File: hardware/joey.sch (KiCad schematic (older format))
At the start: 0 parts

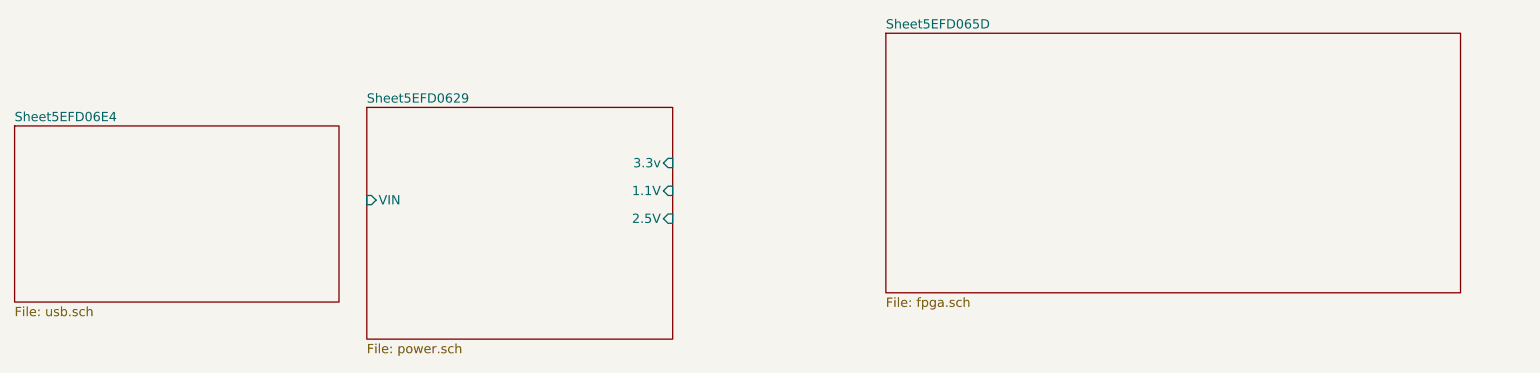
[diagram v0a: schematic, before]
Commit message: Finish FTDI schematic, add datasheets
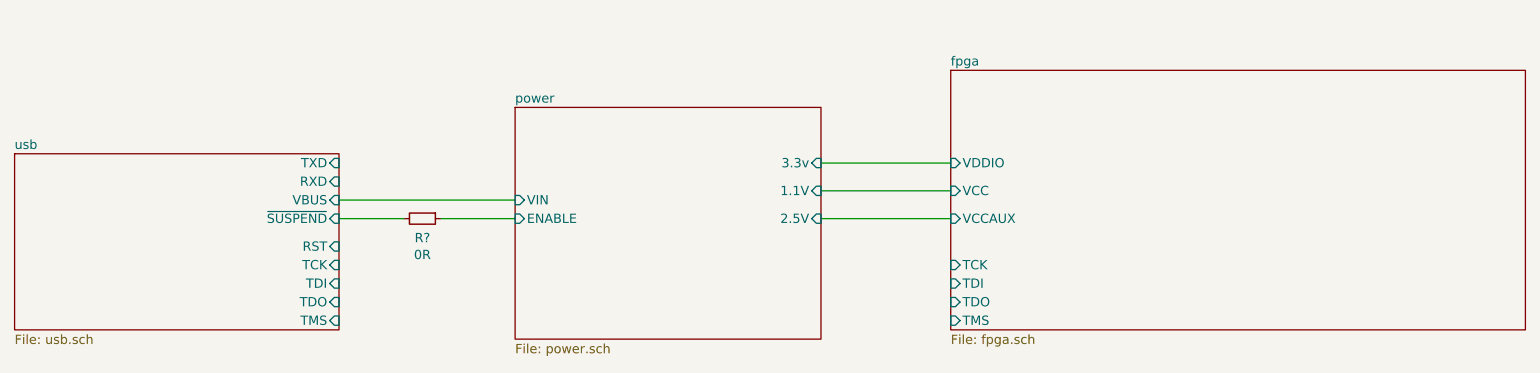
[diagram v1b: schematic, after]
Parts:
- added R?: 0R, symbol Device:R_Small
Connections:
- new net power/ENABLE: R?.1
- new net usb/~SUSPEND~: R?.2
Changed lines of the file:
@@
 $EndDescr
 $Sheet
-S 2650 2450 1650 1250
+S 3450 2450 1650 1250
 U 5EFD062A
-F0 "Sheet5EFD0629" 50
+F0 "power" 50
 F1 "power.sch" 50
-F2 "VIN" I L 2650 2950 50
-F3 "3.3v" I R 4300 2750 50
-F4 "1.1V" I R 4300 2900 50
-F5 "2.5V" I R 4300 3050 50
+F2 "VIN" I L 3450 2950 50
+F3 "3.3v" I R 5100 2750 50
+F4 "1.1V" I R 5100 2900 50
+F5 "2.5V" I R 5100 3050 50
+F6 "ENABLE" I L 3450 3050 50
 $EndSheet
 $Sheet
-S 5450 2050 3100 1400
+S 5800 2250 3100 1400
 U 5EFD065E
-F0 "Sheet5EFD065D" 50
+F0 "fpga" 50
 F1 "fpga.sch" 50
+F2 "VCCAUX" I L 5800 3050 50
+F3 "VCC" I L 5800 2900 50
+F4 "TDO" I L 5800 3500 50
+F5 "TDI" I L 5800 3400 50
+F6 "TCK" I L 5800 3300 50
+F7 "TMS" I L 5800 3600 50
+F8 "VDDIO" I L 5800 2750 50
 $EndSheet
 $Sheet
-S 750  2550 1750 950
+S 750  2700 1750 950
 U 5EFD06E5
-F0 "Sheet5EFD06E4" 50
+F0 "usb" 50
 F1 "usb.sch" 50
+F2 "VBUS" I R 2500 2950 50
+F3 "TCK" I R 2500 3300 50
+F4 "TDI" I R 2500 3400 50
+F5 "TDO" I R 2500 3500 50
+F6 "TMS" I R 2500 3600 50
+F7 "RST" I R 2500 3200 50
+F8 "TXD" I R 2500 2750 50
+F9 "RXD" I R 2500 2850 50
+F10 "~SUSPEND~" I R 2500 3050 50
 $EndSheet
+Wire Wire Line
+	3450 2950 2500 2950
+Wire Wire Line
+	2500 3050 2850 3050
+$Comp
+L Device:R_Small R?
+U 1 1 5F23B182
+P 2950 3050
+F 0 "R?" V 3054 3050 50  0000 C CNN
+F 1 "0R" V 3145 3050 50  0000 C CNN
+F 2 "" H 2950 3050 50  0001 C CNN
+F 3 "~" H 2950 3050 50  0001 C CNN
+	1    2950 3050
+	0    1    1    0
+$EndComp
+Wire Wire Line
+	3050 3050 3450 3050
+Wire Wire Line
+	5800 2750 5100 2750
+Wire Wire Line
+	5100 2900 5800 2900
+Wire Wire Line
+	5800 3050 5100 3050
 $EndSCHEMATC

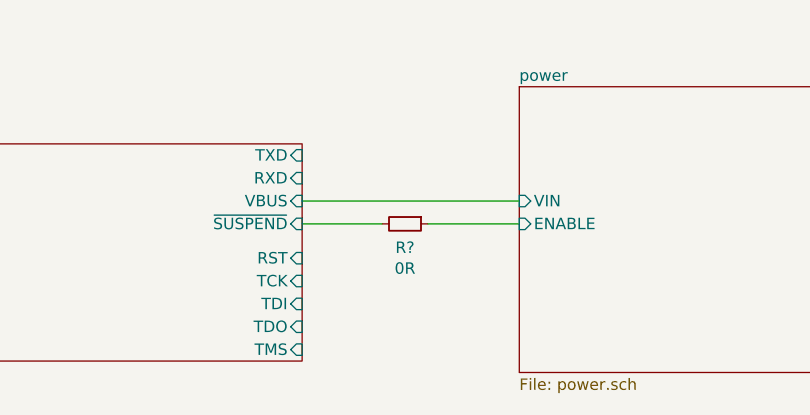
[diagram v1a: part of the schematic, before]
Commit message: Add oscilator, flash, ram
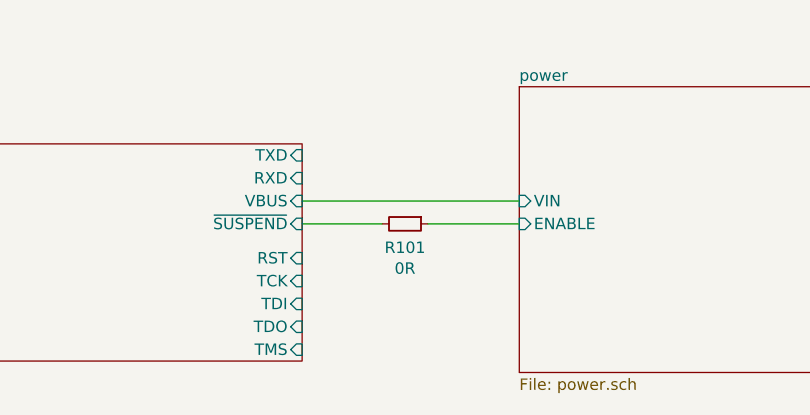
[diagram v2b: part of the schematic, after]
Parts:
- gave numbers to parts that had none: 1
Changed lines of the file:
@@
 EELAYER 30 0
 EELAYER END
-$Descr A4 11693 8268
+$Descr A3 16535 11693
 encoding utf-8
 Sheet 1 4
-Title ""
+Title "Joey"
 Date ""
 Rev ""
@@
 	2500 3050 2850 3050
 $Comp
-L Device:R_Small R?
+L Device:R_Small R101
 U 1 1 5F23B182
 P 2950 3050
-F 0 "R?" V 3054 3050 50  0000 C CNN
+F 0 "R101" V 3054 3050 50  0000 C CNN
 F 1 "0R" V 3145 3050 50  0000 C CNN
 F 2 "" H 2950 3050 50  0001 C CNN

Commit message: More stuff
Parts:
- R101: footprint (none) -> Resistor_SMD:R_0603_1608Metric
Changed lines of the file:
@@
 F 0 "R101" V 3054 3050 50  0000 C CNN
 F 1 "0R" V 3145 3050 50  0000 C CNN
-F 2 "" H 2950 3050 50  0001 C CNN
+F 2 "Resistor_SMD:R_0603_1608Metric" H 2950 3050 50  0001 C CNN
 F 3 "~" H 2950 3050 50  0001 C CNN
 	1    2950 3050
